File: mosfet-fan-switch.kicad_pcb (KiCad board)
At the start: 2 copper layers, 56 x 92 mm, 30 parts, among them J1 12V IN, J3 FAN OUT, J4 NUC FAN HEADER, J5 FTDI HEADER, J6 ICSP, Q1 irfz44n, Q2 2n7002, Q3 irf7416, Q4 BC547, U1 Arduino_Pro_Mini_3V3

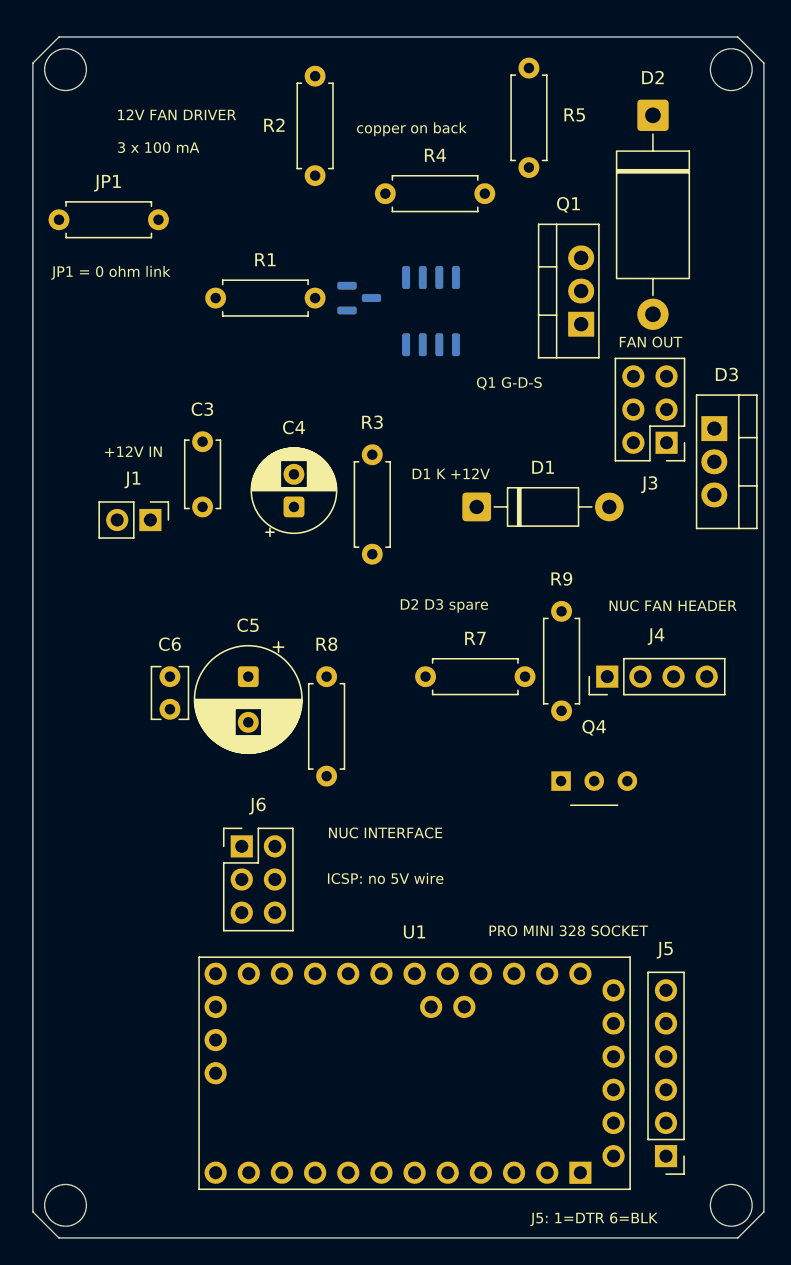
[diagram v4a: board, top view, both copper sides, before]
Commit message: pcb: state the fab rules in the generator, pour /GND and /P12V, park a maze router
build_board.py now declares the prototype limits it is designed against - 0.30 mm clearance and signal track, 1.5 mm power, 0.40/0.80 mm via - and gives /P12V, /GND and /DRAIN their own net classes. Pad numbers are the real package pin numbers rather than the schematic symbol's SPICE order. The regenerated board gains two zone definitions (/GND on B.Cu, /P12V on F.Cu) and is still a placement skeleton with no tracks. router.py is a 0.254 mm grid A* router with 5.08 mm 0 ohm jumper hops, for the single-layer variant. Courtyard DRC severities are relaxed because the Pro Mini socket courtyards necessarily overlap the header holes.
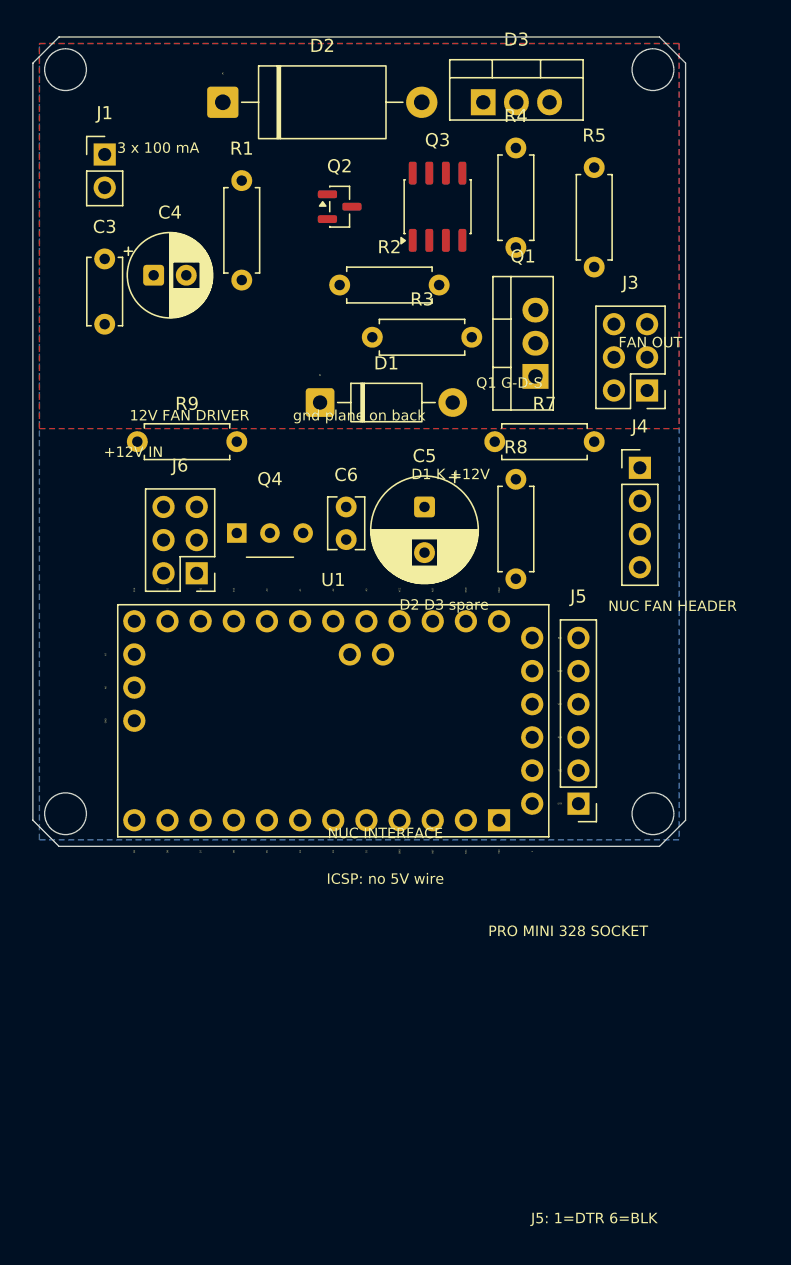
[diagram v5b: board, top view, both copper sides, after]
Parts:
- removed JP1: R, Resistor_THT:R_Axial_DIN0207_L6.3mm_D2.5mm_P7.62mm_Horizontal
- Q2, Q3: moved to F.Cu
- moved R9 35.0 mm to (8.00, 31.0), turned to 0 degrees
- moved D2 33.0 mm to (14.6, 5.00), turned to 0 degrees
- moved Q4 31.3 mm to (15.6, 38.0)
- moved D3 30.6 mm to (34.5, 5.00), turned to 0 degrees
- moved ? 30.6 mm to (47.5, 59.5)
- moved ? 30.0 mm to (2.50, 59.5)
- moved J1 28.2 mm to (5.50, 9.00), turned to 0 degrees
- moved J5 27.8 mm to (41.8, 58.7)
- moved U1 27.7 mm to (7.77, 60.0)
- moved J6 21.2 mm to (12.6, 41.1), turned to -180 degrees
- moved C4 20.8 mm to (9.25, 18.2), turned to 0 degrees
- moved C3 20.4 mm to (5.50, 17.0), turned to -90 degrees
- moved R7 18.8 mm to (43.0, 31.0)
- moved C5 18.7 mm to (30.0, 36.0)
- moved C6 18.7 mm to (24.0, 36.0)
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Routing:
- added copper zone on B.Cu, net /GND
- added copper zone on F.Cu, net /P12V
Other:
- board size 56 x 92 mm -> 50 x 62 mm
- board text added: "gnd plane on back"
- board text removed: "JP1 = 0 ohm link"
- board text removed: "copper on back"
